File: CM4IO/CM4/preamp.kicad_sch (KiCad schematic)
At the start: 23 parts, among them IC1 OPA659IDBVR, IC2 OPA659IDBVR, IC3 LMH6643MAX_NOPB, J1 901-144-8RFX

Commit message: Completed H7/CM4IO Board
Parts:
- removed J1: 901-144-8RFX, 9011448RFX, symbol SamacSys_Parts:901-144-8RFX
- added J1: Conn_Coaxial, Connector_Coaxial:SMA_Samtec_SMA-J-P-H-ST-EM1_EdgeMount, symbol Connector:Conn_Coaxial
- added J6: Conn_01x02_Female, Connector_PinHeader_2.54mm:PinHeader_1x02_P2.54mm_Horizontal, symbol Connector:Conn_01x02_Female
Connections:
- net GND: now also J1.2 (Ext), J6.2 (Pin_2)
- net v_DIV_OUT: now also J6.1 (Pin_1)
- net at R4.2: now also J1.1 (In)
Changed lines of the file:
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@@
     (title "90 - 150KHz 40dB band pass pre-amp")
   )
-  (junction (at 43.434 61.1124) (diameter 1.016) (color 0 0 0 0))
-  (junction (at 63.754 56.0324) (diameter 1.016) (color 0 0 0 0))
+  (junction (at 59.7408 81.8388) (diameter 1.016) (color 0 0 0 0))
   (junction (at 76.708 152.8064) (diameter 1.016) (color 0 0 0 0))
   (junction (at 78.994 61.1124) (diameter 1.016) (color 0 0 0 0))
@@
   (junction (at 174.244 78.8924) (diameter 1.016) (color 0 0 0 0))
   (junction (at 205.994 58.5724) (diameter 1.016) (color 0 0 0 0))
+  (no_connect (at 117.348 152.8064))
+  (no_connect (at 117.348 150.2664))
   (no_connect (at 117.348 147.7264))
-  (no_connect (at 117.348 150.2664))
-  (no_connect (at 117.348 152.8064))
-  (wire (pts (xy 43.434 58.5724) (xy 43.434 61.1124))
-    (stroke (width 0) (type solid) (color 0 0 0 0))
-  )
-  (wire (pts (xy 63.754 56.0324) (xy 63.754 58.5724))
+  (wire (pts (xy 58.42 81.8388) (xy 59.7408 81.8388))
+    (stroke (width 0) (type solid) (color 0 0 0 0))
+  )
+  (wire (pts (xy 59.7408 81.8388) (xy 59.7408 83.7184))
+    (stroke (width 0) (type solid) (color 0 0 0 0))
+  )
+  (wire (pts (xy 59.7408 81.8388) (xy 60.96 81.8388))
+    (stroke (width 0) (type solid) (color 0 0 0 0))
+  )
+  (wire (pts (xy 59.7408 86.2584) (xy 59.7408 83.7184))
+    (stroke (width 0) (type solid) (color 0 0 0 0))
+  )
+  (wire (pts (xy 60.96 61.1124) (xy 63.754 61.1124))
+    (stroke (width 0) (type solid) (color 0 0 0 0))
+  )
+  (wire (pts (xy 60.96 61.5188) (xy 60.96 61.1124))
     (stroke (width 0) (type solid) (color 0 0 0 0))
   )
@@
   )
   (wire (pts (xy 134.874 81.4324) (xy 134.874 62.3824))
+    (stroke (width 0) (type solid) (color 0 0 0 0))
+  )
+  (wire (pts (xy 137.1092 124.1552) (xy 137.922 124.1552))
+    (stroke (width 0) (type solid) (color 0 0 0 0))
+  )
+  (wire (pts (xy 137.922 124.1552) (xy 137.922 127.4064))
+    (stroke (width 0) (type solid) (color 0 0 0 0))
+  )
+  (wire (pts (xy 137.922 127.4064) (xy 138.5316 127.4064))
     (stroke (width 0) (type solid) (color 0 0 0 0))
   )
@@
     (effects (font (size 1.27 1.27)) (justify left))
   )
+  (hierarchical_label "v_DIV_OUT" (shape output) (at 137.1092 124.1552 180)
+    (effects (font (size 1.27 1.27)) (justify right))
+  )
   (hierarchical_label "VPOS" (shape input) (at 189.484 48.5648 90)
     (effects (font (size 1.27 1.27)) (justify left))
@@
     (effects (font (size 1.27 1.27)) (justify right))
   )
-  (symbol (lib_id "power:GND") (at 43.434 61.1124 0) (unit 1)
-    (in_bom yes) (on_board yes)
-    (property "Reference" "#PWR0105" (id 0) (at 43.434 67.4624 0)
-      (effects (font (size 1.27 1.27)) hide)
-    )
-    (property "Value" "GND" (id 1) (at 43.561 65.5066 0))
-    (property "Footprint" "" (id 2) (at 43.434 61.1124 0)
-      (effects (font (size 1.27 1.27)) hide)
-    )
-    (property "Datasheet" "" (id 3) (at 43.434 61.1124 0)
-      (effects (font (size 1.27 1.27)) hide)
-    )
-  )
-  (symbol (lib_id "power:GND") (at 63.754 56.0324 180) (unit 1)
-    (in_bom yes) (on_board yes)
-    (property "Reference" "#PWR0106" (id 0) (at 63.754 49.6824 0)
-      (effects (font (size 1.27 1.27)) hide)
-    )
-    (property "Value" "GND" (id 1) (at 63.627 51.6382 0))
-    (property "Footprint" "" (id 2) (at 63.754 56.0324 0)
-      (effects (font (size 1.27 1.27)) hide)
-    )
-    (property "Datasheet" "" (id 3) (at 63.754 56.0324 0)
+  (symbol (lib_id "power:GND") (at 55.88 66.5988 0) (unit 1)
+    (in_bom yes) (on_board yes)
+    (property "Reference" "#PWR0105" (id 0) (at 55.88 72.9488 0)
+      (effects (font (size 1.27 1.27)) hide)
+    )
+    (property "Value" "GND" (id 1) (at 56.007 70.993 0))
+    (property "Footprint" "" (id 2) (at 55.88 66.5988 0)
+      (effects (font (size 1.27 1.27)) hide)
+    )
+    (property "Datasheet" "" (id 3) (at 55.88 66.5988 0)
+      (effects (font (size 1.27 1.27)) hide)
+    )
+  )
+  (symbol (lib_id "power:GND") (at 59.7408 86.2584 0) (unit 1)
+    (in_bom yes) (on_board yes)
+    (property "Reference" "#PWR0106" (id 0) (at 59.7408 92.6084 0)
+      (effects (font (size 1.27 1.27)) hide)
+    )
+    (property "Value" "GND" (id 1) (at 59.8678 90.6526 0))
+    (property "Footprint" "" (id 2) (at 59.7408 86.2584 0)
+      (effects (font (size 1.27 1.27)) hide)
+    )
+    (property "Datasheet" "" (id 3) (at 59.7408 86.2584 0)
       (effects (font (size 1.27 1.27)) hide)
     )
@@
     )
     (property "Datasheet" "" (id 3) (at 102.108 160.4264 0)
+      (effects (font (size 1.27 1.27)) hide)
+    )
+  )
+  (symbol (lib_id "power:GND") (at 138.5316 129.9464 0) (unit 1)
+    (in_bom yes) (on_board yes)
+    (property "Reference" "#PWR04" (id 0) (at 138.5316 136.2964 0)
+      (effects (font (size 1.27 1.27)) hide)
+    )
+    (property "Value" "GND" (id 1) (at 138.6586 134.3406 0))
+    (property "Footprint" "" (id 2) (at 138.5316 129.9464 0)
+      (effects (font (size 1.27 1.27)) hide)
+    )
+    (property "Datasheet" "" (id 3) (at 138.5316 129.9464 0)
       (effects (font (size 1.27 1.27)) hide)
     )
@@
     )
   )
-  (symbol (lib_id "SamacSys_Parts:901-144-8RFX") (at 63.754 61.1124 180) (unit 1)
-    (in_bom yes) (on_board yes)
-    (property "Reference" "J1" (id 0) (at 53.594 49.333 0))
-    (property "Value" "901-144-8RFX" (id 1) (at 53.594 51.6317 0))
-    (property "Footprint" "9011448RFX" (id 2) (at 47.244 63.6524 0)
-      (effects (font (size 1.27 1.27)) (justify left) hide)
-    )
-    (property "Datasheet" "https://componentsearchengine.com/Datasheets/1/901-144-8RFX.pdf" (id 3) (at 47.244 61.1124 0)
-      (effects (font (size 1.27 1.27)) (justify left) hide)
-    )
-    (property "Description" "AMPHENOL RF - 901-144-8RFX - RF / Coaxial Connector, SMA Coaxial, Straight Jack, Solder, 50 ohm, Beryllium Copper" (id 4) (at 47.244 58.5724 0)
-      (effects (font (size 1.27 1.27)) (justify left) hide)
-    )
-    (property "Height" "9.53" (id 5) (at 47.244 56.0324 0)
-      (effects (font (size 1.27 1.27)) (justify left) hide)
-    )
-    (property "Manufacturer_Name" "Amphenol" (id 6) (at 47.244 53.4924 0)
-      (effects (font (size 1.27 1.27)) (justify left) hide)
-    )
-    (property "Manufacturer_Part_Number" "901-144-8RFX" (id 7) (at 47.244 50.9524 0)
-      (effects (font (size 1.27 1.27)) (justify left) hide)
-    )
-    (property "Arrow Part Number" "901-144-8RFX" (id 8) (at 47.244 48.4124 0)
-      (effects (font (size 1.27 1.27)) (justify left) hide)
-    )
-    (property "Arrow Price/Stock" "https://www.arrow.com/en/products/901-144-8rfx/amphenol-rf" (id 9) (at 47.244 45.8724 0)
-      (effects (font (size 1.27 1.27)) (justify left) hide)
-    )
-    (property "Mouser Part Number" "523-901-144-8RFX" (id 10) (at 47.244 43.3324 0)
-      (effects (font (size 1.27 1.27)) (justify left) hide)
-    )
-    (property "Mouser Price/Stock" "https://www.mouser.co.uk/ProductDetail/Amphenol-RF/901-144-8RFX?qs=jpOL8GWAqat%252BbPjbt8toTg%3D%3D" (id 11) (at 47.244 40.7924 0)
-      (effects (font (size 1.27 1.27)) (justify left) hide)
-    )
-  )
+  (symbol (lib_id "Connector:Conn_01x02_Female") (at 143.6116 127.4064 0) (unit 1)
+    (in_bom yes) (on_board yes)
+    (property "Reference" "J6" (id 0) (at 144.3229 127.9842 0)
+      (effects (font (size 1.27 1.27)) (justify left))
+    )
+    (property "Value" "Conn_01x02_Female" (id 1) (at 144.3229 130.2829 0)
+      (effects (font (size 1.27 1.27)) (justify left))
+    )
+    (property "Footprint" "Connector_PinHeader_2.54mm:PinHeader_1x02_P2.54mm_Horizontal" (id 2) (at 143.6116 127.4064 0)
+      (effects (font (size 1.27 1.27)) hide)
+    )
+    (property "Datasheet" "~" (id 3) (at 143.6116 127.4064 0)
+      (effects (font (size 1.27 1.27)) hide)
+    )
+  )
+  (symbol (lib_id "Connector:Conn_Coaxial") (at 60.96 66.5988 270) (unit 1)
+    (in_bom yes) (on_board yes)
+    (property "Reference" "J1" (id 0) (at 63.5255 63.6714 90)
+      (effects (font (size 1.27 1.27)) (justify left))
+    )
+    (property "Value" "Conn_Coaxial" (id 1) (at 63.5255 65.9701 90)
+      (effects (font (size 1.27 1.27)) (justify left))
+    )
+    (property "Footprint" "Connector_Coaxial:SMA_Samtec_SMA-J-P-H-ST-EM1_EdgeMount" (id 2) (at 60.96 66.5988 0)
+      (effects (font (size 1.27 1.27)) hide)
+    )
+    (property "Datasheet" " ~" (id 3) (at 60.96 66.5988 0)
+      (effects (font (size 1.27 1.27)) hide)
+    )
+  )

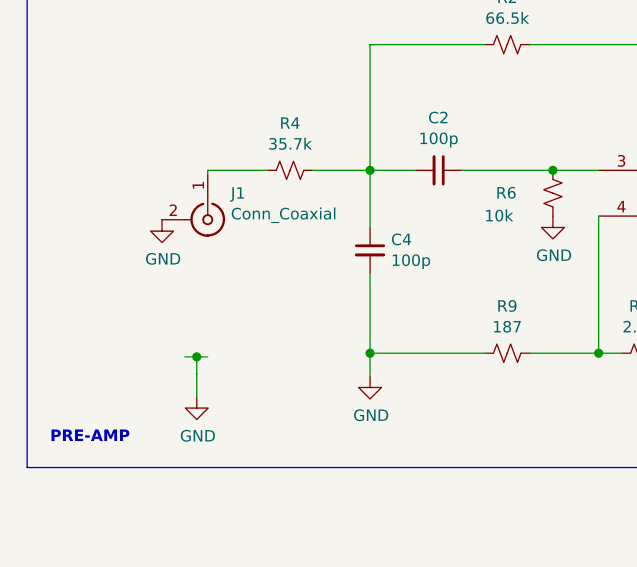
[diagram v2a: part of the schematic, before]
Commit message: Corrected SMPS configuration
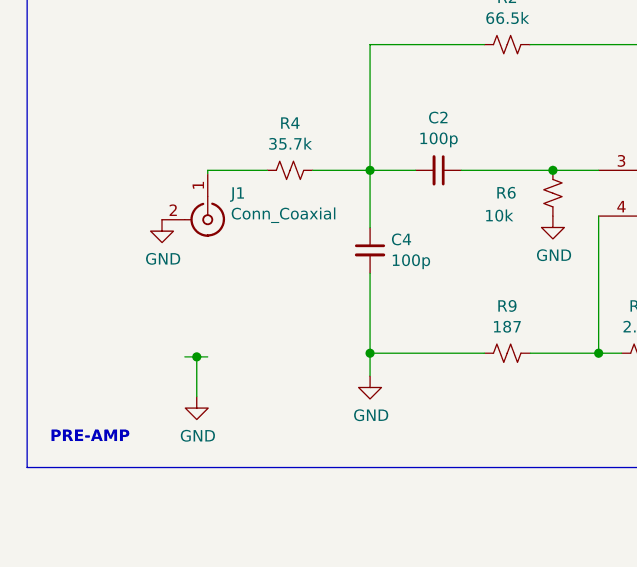
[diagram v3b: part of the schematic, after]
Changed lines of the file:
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@@
   (junction (at 174.244 78.8924) (diameter 1.016) (color 0 0 0 0))
   (junction (at 205.994 58.5724) (diameter 1.016) (color 0 0 0 0))
+  (no_connect (at 117.348 147.7264))
   (no_connect (at 117.348 152.8064))
   (no_connect (at 117.348 150.2664))
-  (no_connect (at 117.348 147.7264))
   (wire (pts (xy 58.42 81.8388) (xy 59.7408 81.8388))
     (stroke (width 0) (type solid) (color 0 0 0 0))
   )
-  (wire (pts (xy 59.7408 81.8388) (xy 59.7408 83.7184))
+  (wire (pts (xy 59.7408 81.8388) (xy 59.7408 86.2584))
     (stroke (width 0) (type solid) (color 0 0 0 0))
   )
@@
     (stroke (width 0) (type solid) (color 0 0 0 0))
   )
-  (wire (pts (xy 59.7408 86.2584) (xy 59.7408 83.7184))
-    (stroke (width 0) (type solid) (color 0 0 0 0))
-  )
-  (wire (pts (xy 60.96 61.1124) (xy 63.754 61.1124))
+  (wire (pts (xy 60.96 61.1124) (xy 67.564 61.1124))
     (stroke (width 0) (type solid) (color 0 0 0 0))
   )
@@
     (stroke (width 0) (type solid) (color 0 0 0 0))
   )
-  (wire (pts (xy 63.754 61.1124) (xy 67.564 61.1124))
-    (stroke (width 0) (type solid) (color 0 0 0 0))
-  )
